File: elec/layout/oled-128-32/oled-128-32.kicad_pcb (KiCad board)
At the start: 2 copper layers, 14 parts

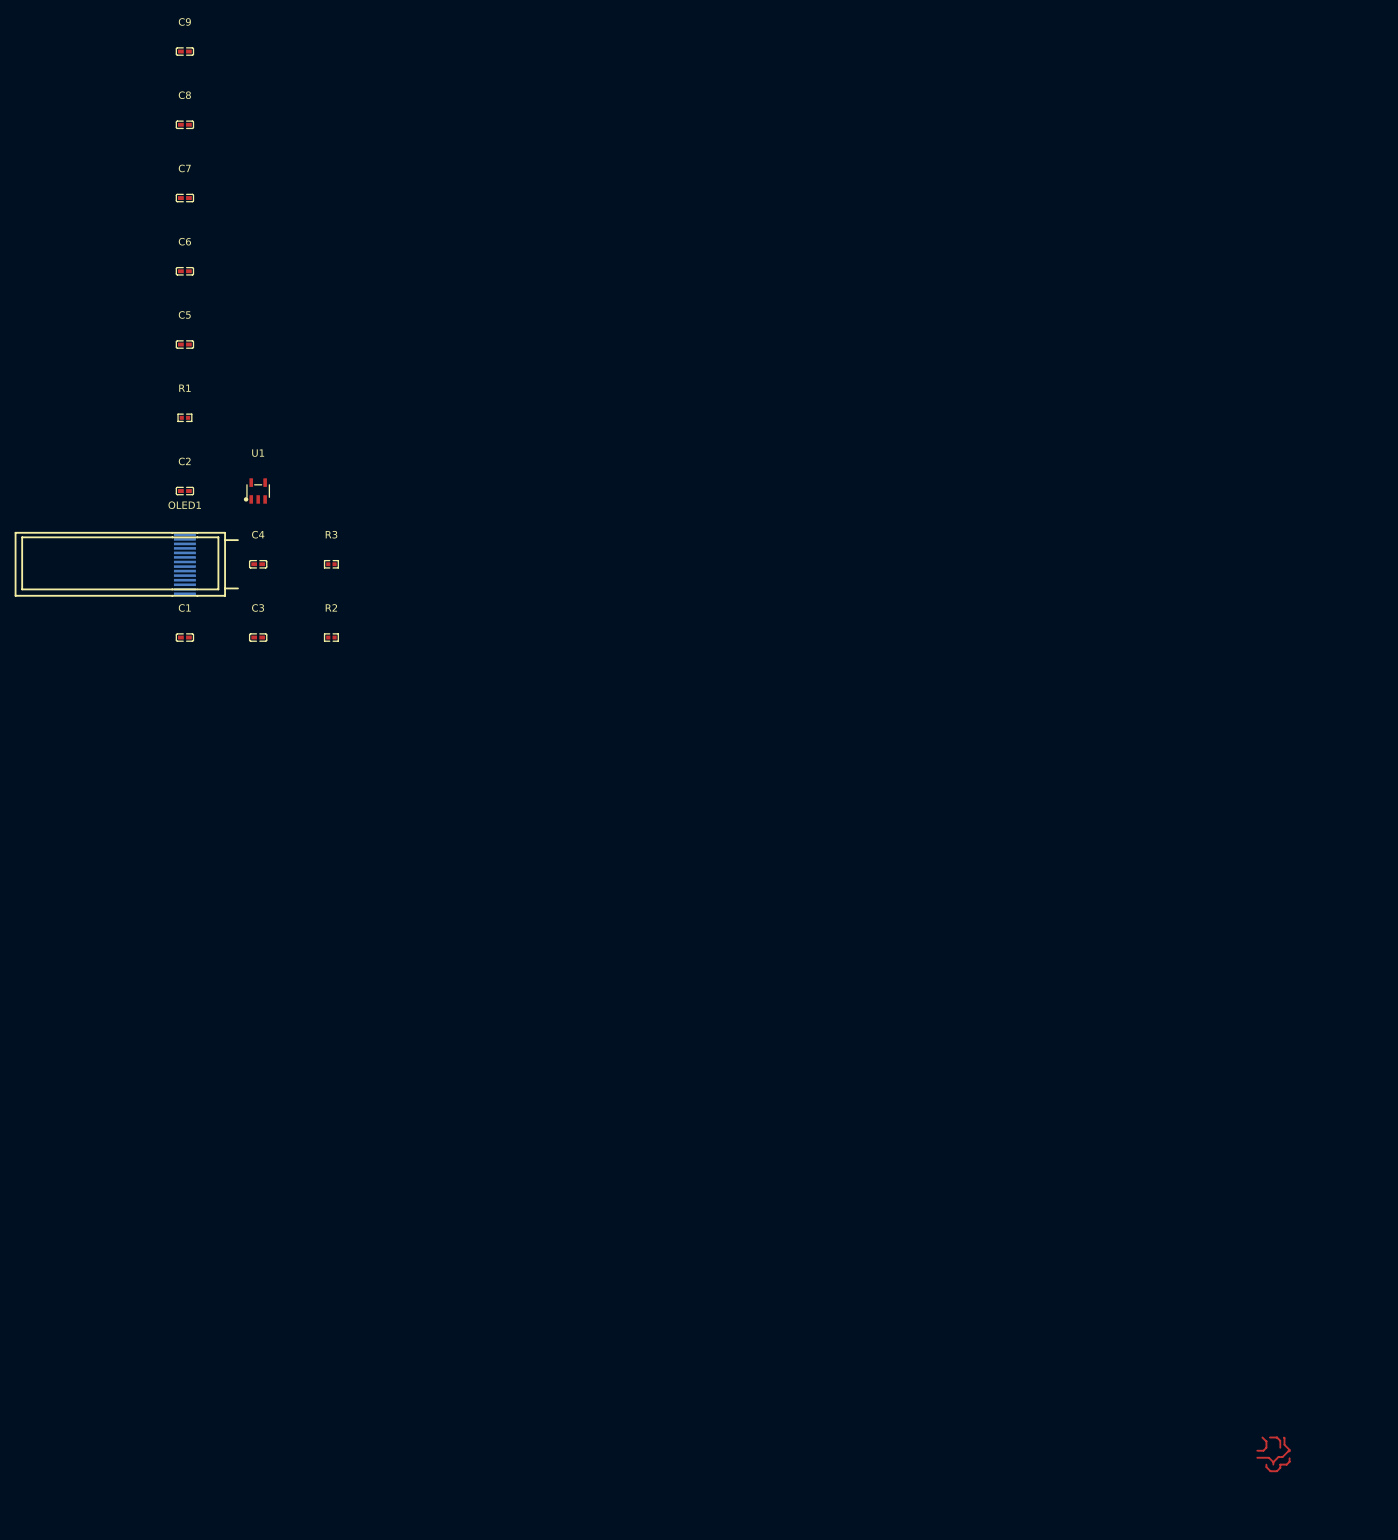
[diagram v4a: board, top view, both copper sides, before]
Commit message: reduce LED brightness on relay and power supply
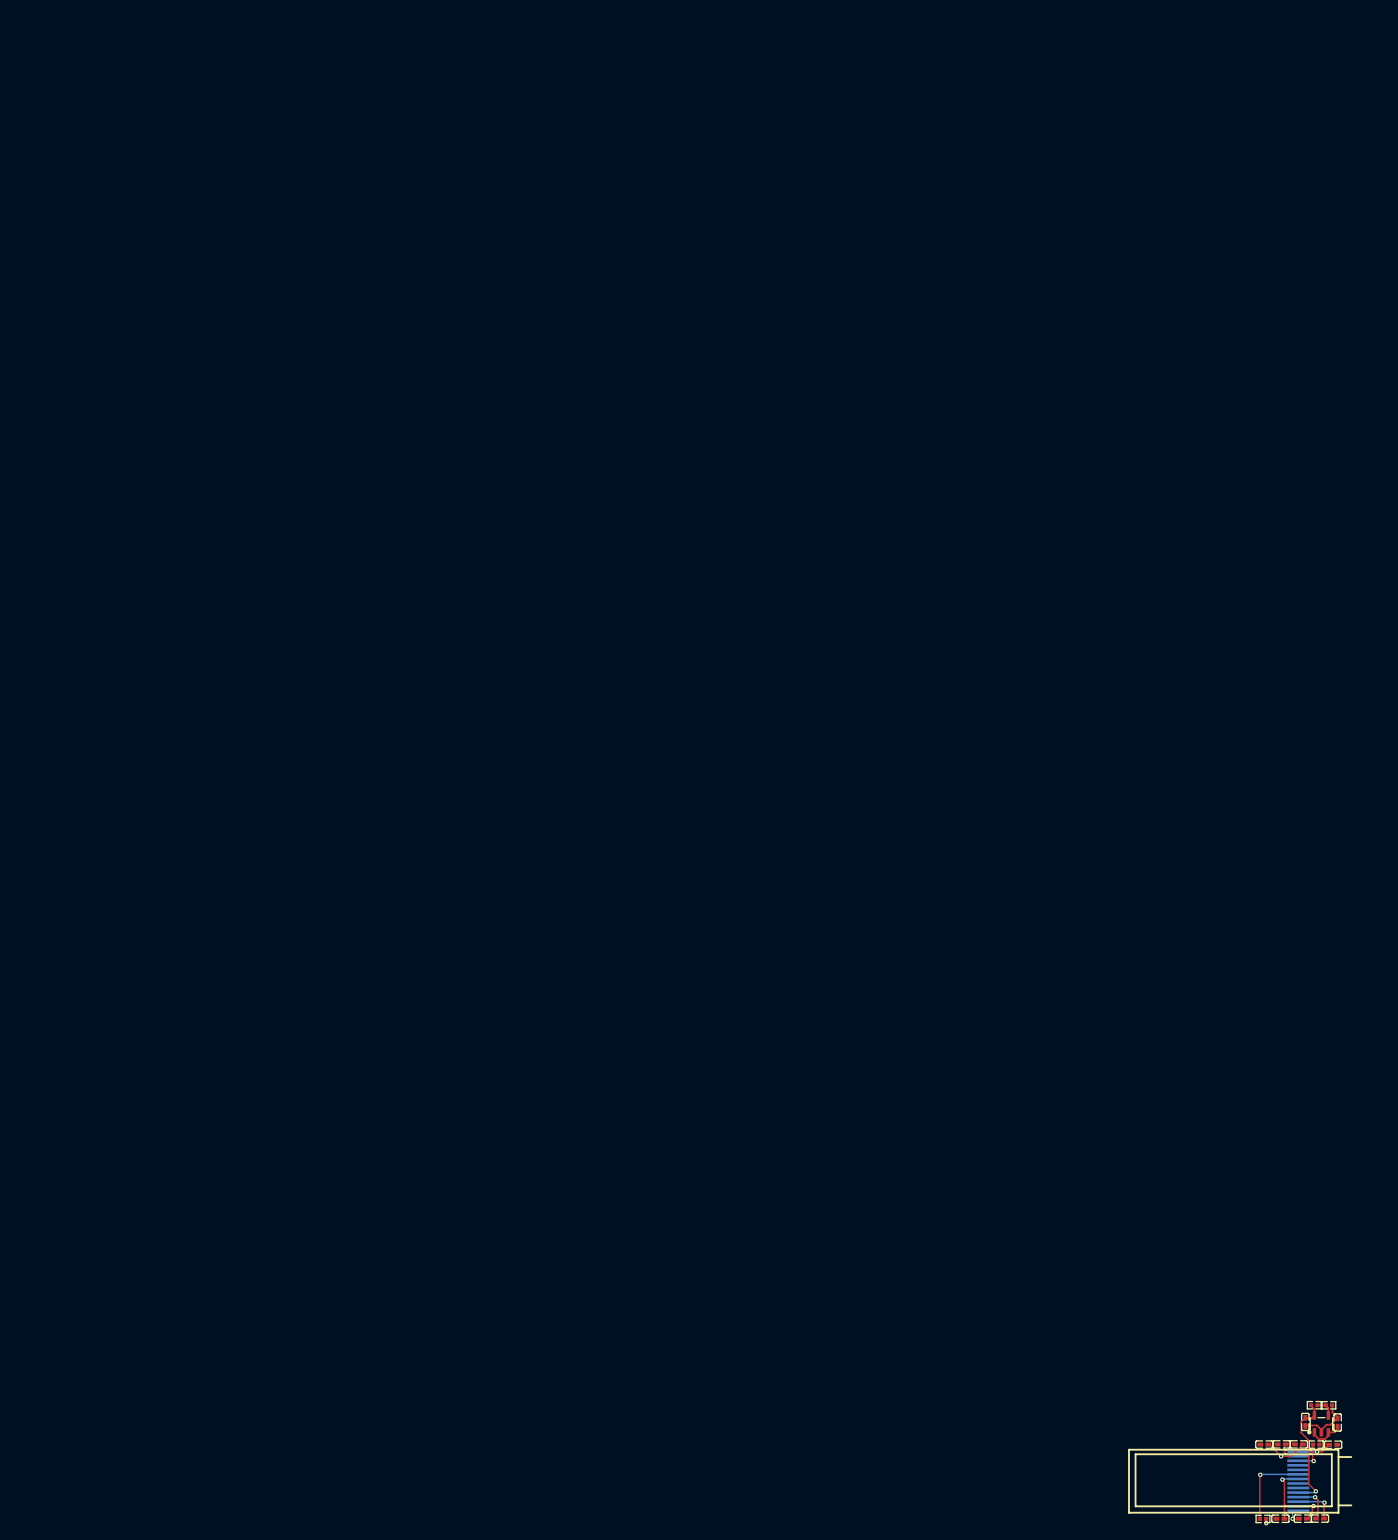
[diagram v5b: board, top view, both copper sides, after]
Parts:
- added R4: 10kΩ ±1% 62.5mW, atopile:R0402-56259e, F.Cu at (147.2, 120.3)
- C6: value 4.7µF ±20% 6.3V X5R -> 4.7µF ±20% 10V X5R
- R2: value 3.9kΩ ±1% 62.5mW -> 10kΩ ±1% 62.5mW
- R3: value 10kΩ ±1% 62.5mW -> 25.5kΩ ±1% 62.5mW
- moved C9 240.6 mm to (147.3, 110.2), turned to 180 degrees
- moved C7 234.3 mm to (149.6, 120.3), turned to 180 degrees
- moved C8 234.2 mm to (149.7, 110.2), turned to 180 degrees
- moved C6 224.1 mm to (156.8, 110.2)
- moved C5 213.7 mm to (152.1, 110.2), turned to 180 degrees
- moved R1 208.6 mm to (154.4, 110.2)
- moved C2 207.3 mm to (152.6, 120.3), turned to 180 degrees
- moved OLED1 196.9 mm to (152.0, 115.2)
- moved C1 196.2 mm to (154.9, 120.3)
- moved U1 193.1 mm to (155.2, 107.3)
- moved C4 184.8 mm to (153.0, 107.1), turned to -90 degrees
- moved C3 182.2 mm to (157.4, 107.2), turned to 90 degrees
- moved R3 176.6 mm to (154.2, 104.8)
- moved R2 171.8 mm to (156.2, 104.8)
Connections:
- C4 pad 1: hv-3 -> hv-2
- C5 pad 1: hv-2 -> hv-1
- C6 pad 1: hv-2 -> hv-1
- C7 pad 1: VCOMH -> hv-1
- OLED1 pad 13: VCOMH -> hv-1
- OLED1 pad 14: hv-2 -> hv-1
- OLED1 pad 5: hv-3 -> hv-2
- R3 pad 1: hv-3 -> hv-2
- U1 pad 5: hv-3 -> hv-2
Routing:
- net hv-1: track 0.00 -> 23.1 mm, vias 0 -> 4
- net (no net): track 18.3 -> 0.00 mm
- net hv-2: track 0.00 -> 16.6 mm, vias 0 -> 1
- net RESh: track 0.00 -> 11.3 mm, vias 0 -> 1
- net gnd: track 0.00 -> 7.73 mm
- net C1P: track 0.00 -> 5.84 mm, vias 0 -> 1
- net C1N: track 0.00 -> 5.49 mm, vias 0 -> 1
- net hv: track 0.00 -> 5.00 mm
- net IREF: track 0.00 -> 4.40 mm, vias 0 -> 1
- net C2N: track 0.00 -> 4.39 mm, vias 0 -> 1
- net C2P: track 0.00 -> 2.68 mm, vias 0 -> 1
- net ADJ_NC: track 0.00 -> 2.56 mm

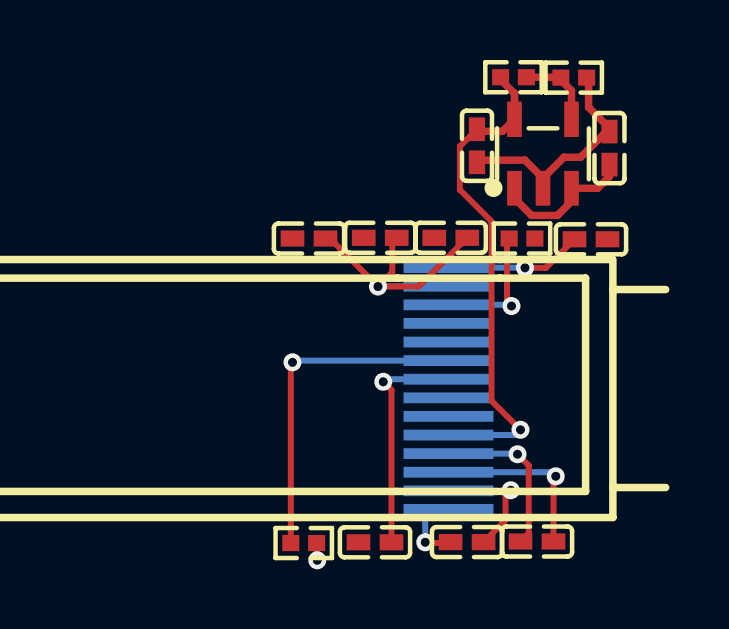
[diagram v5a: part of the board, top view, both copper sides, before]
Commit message: update layout for OLED
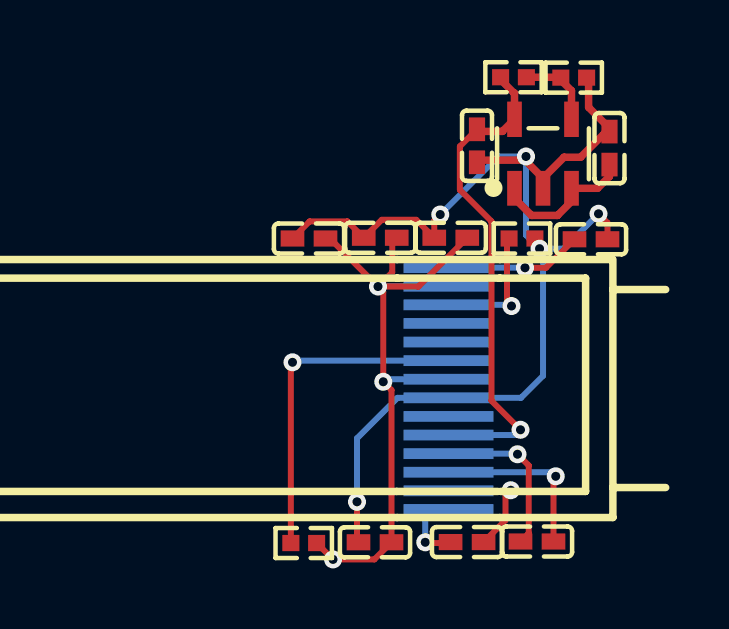
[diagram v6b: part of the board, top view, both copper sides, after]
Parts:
- C6: value 4.7µF ±20% 10V X5R -> 4.7µF ±10% 10V X5R
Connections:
- C4 pad 1: hv-2 -> hv-1
- C5 pad 1: hv-1 -> hv-2
- C6 pad 1: hv-1 -> hv-2
- C7 pad 1: hv-1 -> hv-2
- C8 pad 1: hv-1 -> hv-2
- C9 pad 1: hv-1 -> hv-2
- OLED1 pad 13: hv-1 -> hv-2
- OLED1 pad 14: hv-1 -> hv-2
- OLED1 pad 5: hv-2 -> hv-1
- OLED1 pad 8: hv-1 -> hv-2
- R3 pad 1: hv-2 -> hv-1
- R4 pad 2: hv-1 -> hv-2
- U1 pad 5: hv-2 -> hv-1
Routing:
- net gnd: track 7.73 -> 39.9 mm, vias 0 -> 5
- net hv-2: track 16.6 -> 28.7 mm, vias 1 -> 4
- net hv-1: track 23.1 -> 16.6 mm, vias 4 -> 1

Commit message: checkin
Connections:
- C3 pad 1: hv -> hv-2
- C5 pad 1: hv-2 -> hv
- C6 pad 1: hv-2 -> hv
- C7 pad 1: hv-2 -> hv
- C8 pad 1: hv-2 -> hv
- C9 pad 1: hv-2 -> hv
- OLED1 pad 13: hv-2 -> hv
- OLED1 pad 14: hv-2 -> hv
- OLED1 pad 8: hv-2 -> hv
- R4 pad 2: hv-2 -> hv
- U1 pad 1: hv -> hv-2
- U1 pad 3: hv -> hv-2
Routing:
- net hv-2: track 28.7 -> 5.00 mm, vias 4 -> 0
- net hv: track 5.00 -> 28.7 mm, vias 0 -> 4

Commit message: build with excluded checks
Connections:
- C3 pad 1: hv-2 -> hv-1
- C4 pad 1: hv-1 -> hv-2
- OLED1 pad 5: hv-1 -> hv-2
- R3 pad 1: hv-1 -> hv-2
- U1 pad 1: hv-2 -> hv-1
- U1 pad 3: hv-2 -> hv-1
- U1 pad 5: hv-1 -> hv-2
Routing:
- net hv-2: track 5.00 -> 16.6 mm, vias 0 -> 1
- net hv-1: track 16.6 -> 5.00 mm, vias 1 -> 0
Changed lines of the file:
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@@
     (net 3 "SCL")
     (net 4 "C1P")
-    (net 5 "hv-1")
+    (net 5 "hv-2")
     (net 6 "ADJ_NC")
     (net 7 "C2P")
@@
     (net 10 "C1N")
     (net 11 "SDA")
-    (net 12 "hv-2")
+    (net 12 "hv-1")
     (net 13 "RESh")
     (net 14 "hv")
@@
             (size 0.57 0.54)
             (layers "F.Cu" "F.Mask" "F.Paste")
-            (net 5 "hv-1")
+            (net 5 "hv-2")
         )
         (pad "2" smd rect
@@
             (size 0.49 1.16)
             (layers "F.Cu" "F.Mask" "F.Paste")
-            (net 12 "hv-2")
+            (net 12 "hv-1")
         )
         (pad "2" smd rect
@@
             (size 0.49 1.16)
             (layers "F.Cu" "F.Mask" "F.Paste")
-            (net 12 "hv-2")
+            (net 12 "hv-1")
         )
         (pad "4" smd rect
@@
             (size 0.49 1.18)
             (layers "F.Cu" "F.Mask" "F.Paste")
-            (net 5 "hv-1")
+            (net 5 "hv-2")
         )
         (embedded_fonts no)
@@
             (size 0.79 0.54)
             (layers "F.Cu" "F.Mask" "F.Paste")
-            (net 5 "hv-1")
+            (net 5 "hv-2")
         )
         (pad "2" smd rect
@@
             (size 3 0.36)
             (layers "B.Cu" "B.Mask" "B.Paste")
-            (net 5 "hv-1")
+            (net 5 "hv-2")
         )
         (pad "6" smd rect
@@
             (size 0.79 0.54)
             (layers "F.Cu" "F.Mask" "F.Paste")
-            (net 12 "hv-2")
+            (net 12 "hv-1")
         )
         (pad "2" smd rect
